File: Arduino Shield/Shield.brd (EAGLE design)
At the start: 54.6 x 53.3 mm, 5 parts

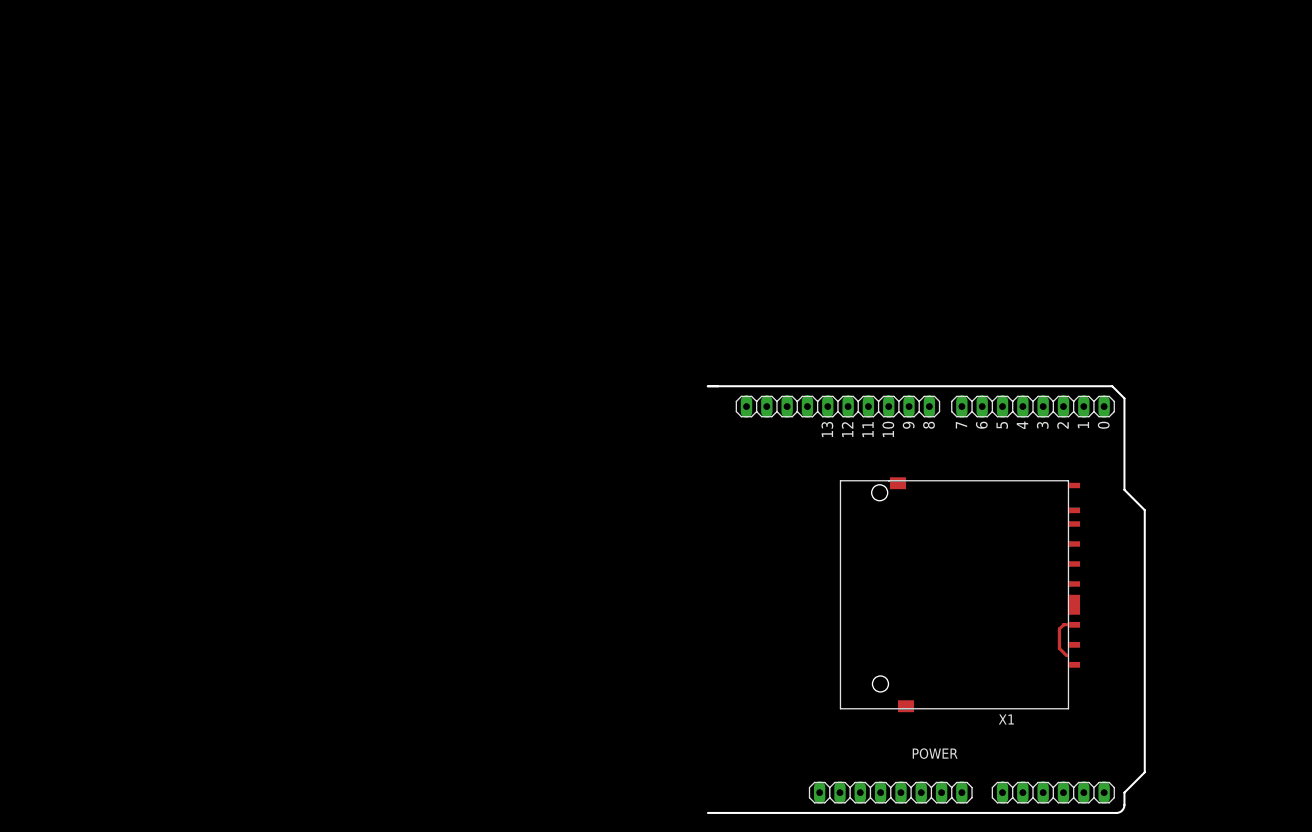
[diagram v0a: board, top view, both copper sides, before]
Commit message: Schem of shield
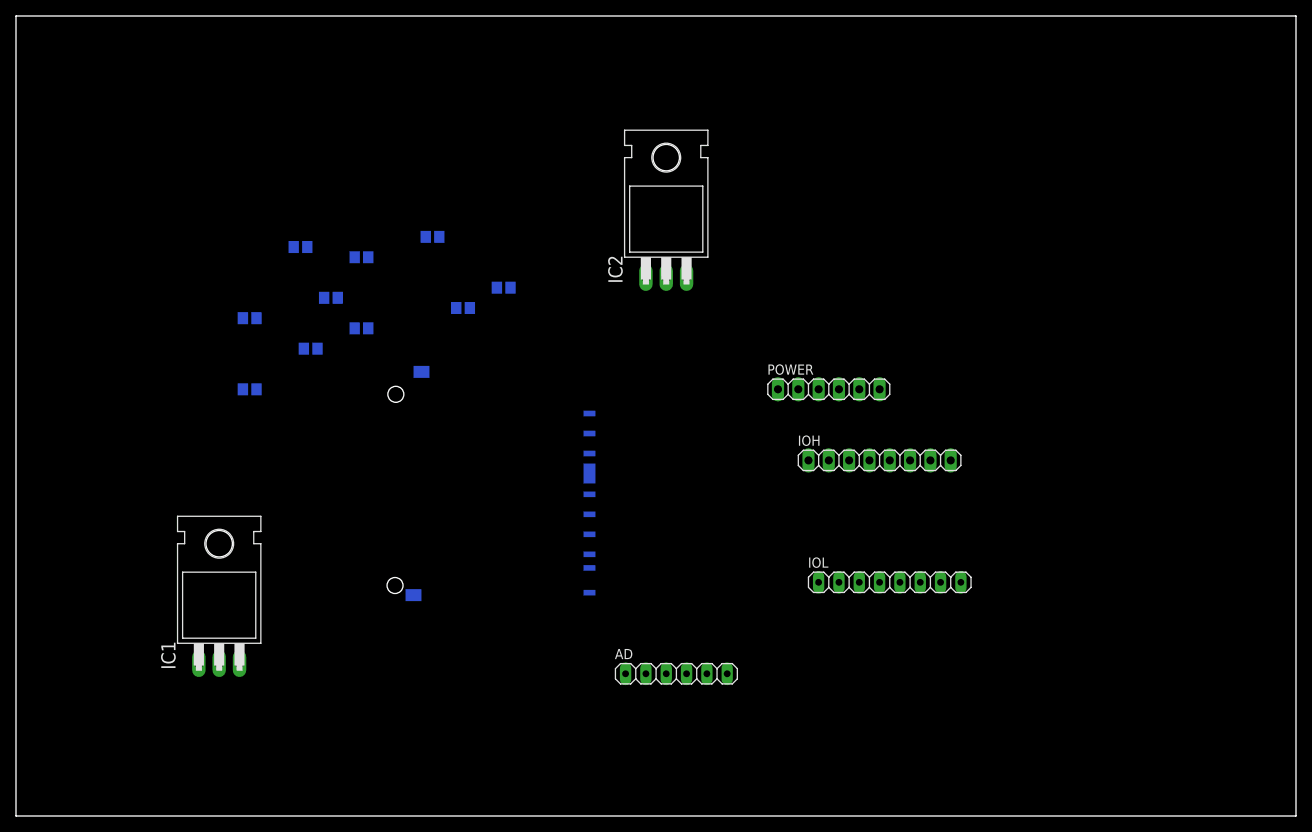
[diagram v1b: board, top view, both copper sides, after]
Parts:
- added 750, R8: 910, resistor:R0805
- added IC1, IC2: 317T, linear:TO220H
- added R1, R2, R3: 1.8k, resistor:R0805
- added R4, R5, R6: 3.3k, resistor:R0805
- added R7, R9: 240, resistor:R0805
- AD: device SmartPrj:1X06 -> SmartPrj:1X06@1
- IOH: device SmartPrj:1X10@1 -> pinhead:1X08
- IOL: device SmartPrj:1X08 -> SmartPrj:1X08@1
- POWER: device SmartPrj:1X08 -> pinhead:1X06
- moved X1 62.3 mm to (55.9, 41.9), flipped to the bottom, turned to 0 degrees
- moved POWER 51.0 mm to (101.6, 53.3)
- moved AD 49.4 mm to (82.5, 17.8)
- moved IOL 28.3 mm to (109.2, 29.2), turned to 0 degrees
- moved IOH 8.51 mm to (108.0, 44.5), turned to 0 degrees
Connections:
- removed net S$3: X1.CLK(CLK)
- new net 3.3V: POWER.2, X1.VDD(VCC)
- new net 5V: IC2.2, POWER.3, R9.1
- new net 6V: IC1.2, R7.1
- new net N$1: IC1.1, R7.2, R8.1
- new net N$2: 750.1, IC2.1, R9.2
- new net PIN11: IOH.4, R1.1
- new net PIN12: IOH.5, X1.(DATA0)D0
- new net PIN13: IOH.6, R3.1
- new net PIN4: IOL.5, R2.1
- new net RESET: POWER.1
- new net SD_CLK: R3.2, R4.1, X1.CLK(CLK)
- new net SD_CS: R2.2, R5.1, X1.CD/DATA3(CS)
- new net V_IN: IC1.3, IC2.3
- new net V_INPUT: POWER.6
- net GND: now also 750.2, POWER.4, POWER.5, R4.2, R5.2, R6.2, R8.2
- net SD_DI: now also R1.2, R6.1
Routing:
- net SD_DI: track 5.72 -> 0.00 mm
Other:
- board size 54.6 x 53.3 mm -> 160 x 100 mm
- board text removed: "0"
- board text removed: "1"
- board text removed: "10"
- board text removed: "11"
- board text removed: "12"
- board text removed: "13"
- board text removed: "2"
- board text removed: "3"
- board text removed: "4"
- board text removed: "5"
- board text removed: "6"
- board text removed: "7"
- board text removed: "8"
- board text removed: "9"
